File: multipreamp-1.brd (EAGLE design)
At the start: 100 x 50 mm, 132 parts, among them Q1 J201, Q2 J201, Q3 J201, Q4 J201, Q5 2N5088, Q6 J201, Q7 J201, Q8 J201

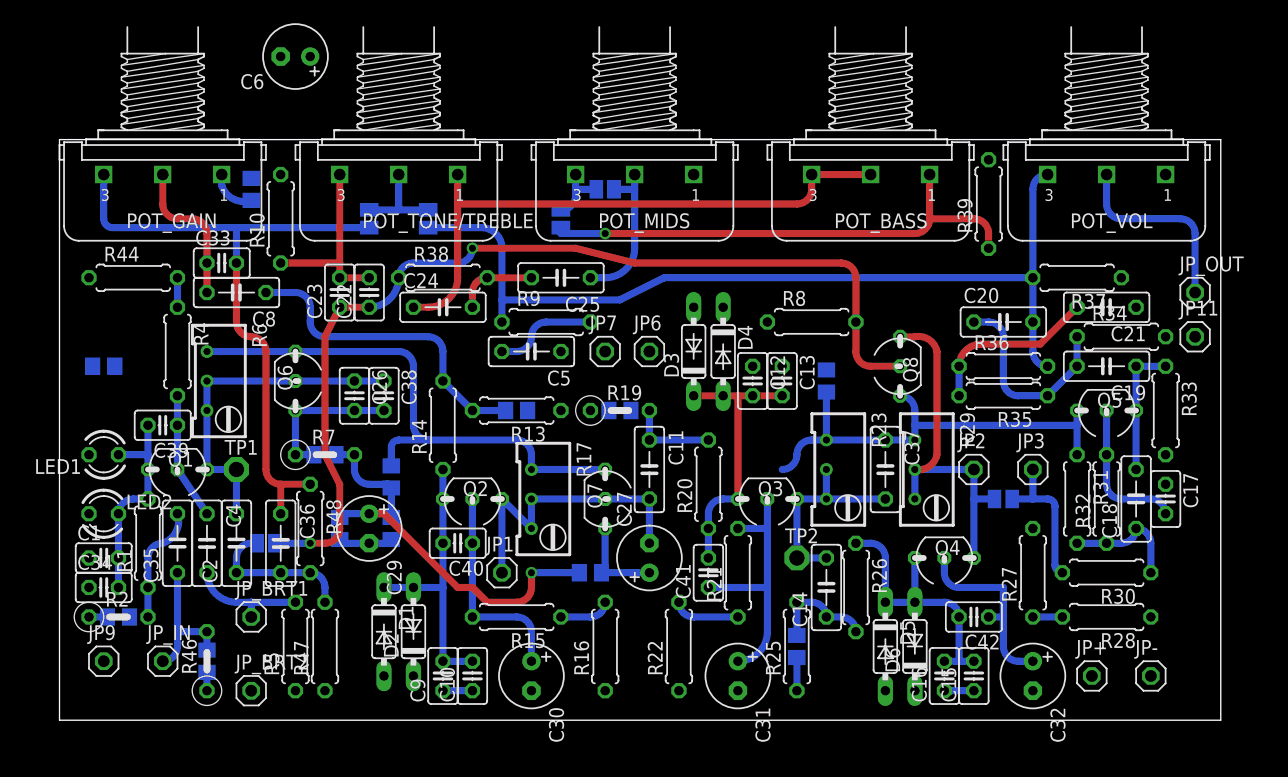
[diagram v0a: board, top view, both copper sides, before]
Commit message: Adicao de filtros RC na alimentacao (esquematico e layout)
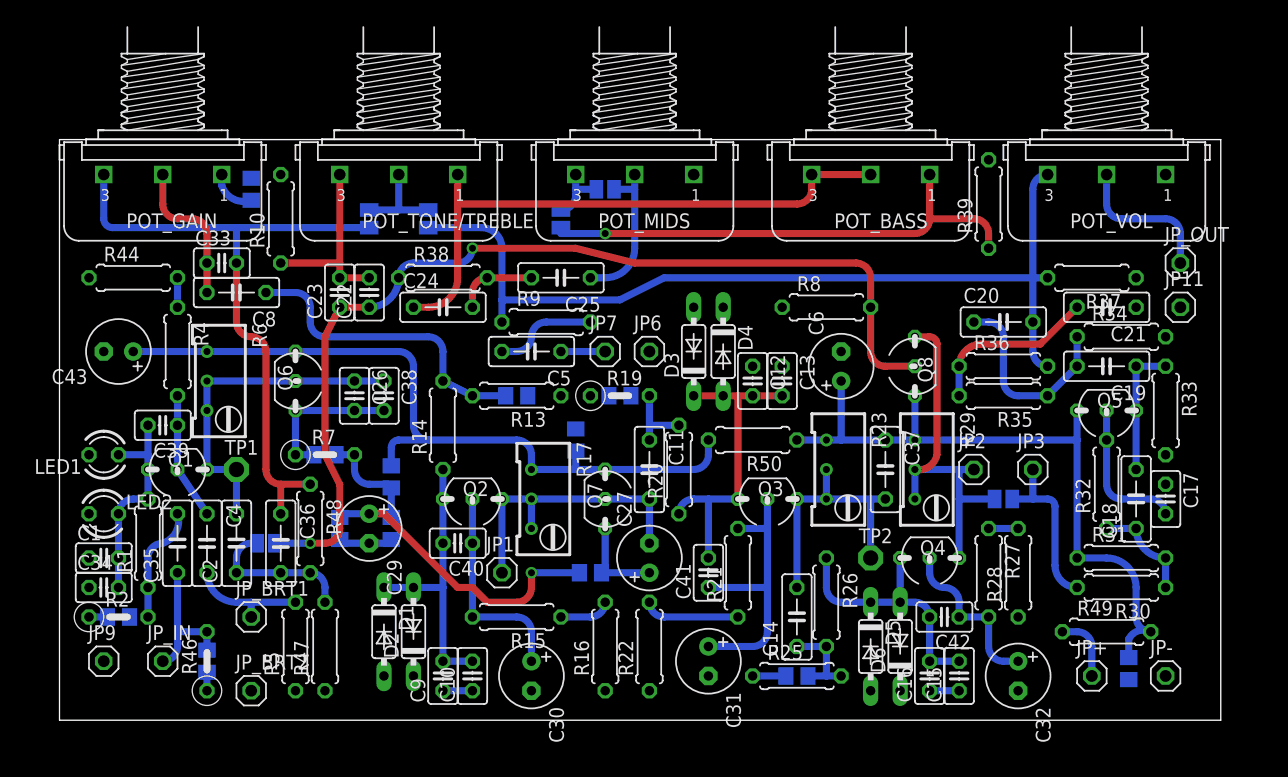
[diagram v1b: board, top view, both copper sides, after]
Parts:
- added C43: (no value), rcl:E2,5-6
- added R49, R50: (no value), rcl:0207/7
- moved C3 92.0 mm to (92.1, 4.45), turned to 270 degrees
- moved C6 54.0 mm to (67.3, 30.5), turned to 90 degrees
- moved C7 22.2 mm to (44.5, 24.1)
- moved R28 8.52 mm to (82.5, 12.7), turned to 90 degrees
- moved R31 6.35 mm to (91.4, 14.0), turned to 0 degrees
- moved TP2 6.35 mm to (69.8, 14.0)
- moved R27 3.81 mm to (80.0, 12.7), turned to 270 degrees
- moved C14 3.59 mm to (63.5, 8.89)
- moved JP11 2.84 mm to (96.5, 35.6)
- moved JP_OUT 2.84 mm to (96.5, 39.4)
- moved C31 2.84 mm to (55.9, 5.08)
- moved R20 2.84 mm to (53.3, 21.6)
- moved R26 2.84 mm to (66.0, 10.2)
- moved R22 2.54 mm to (50.8, 6.35)
- moved R24 2.54 mm to (63.5, 3.81), turned to 180 degrees
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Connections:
- new net 9V_1: C3.1, C37.1, C6.+, Q5.1, Q8.3, R23.1, R29.1, R31.1, R49.2, R50.1
- new net N$44: JP+.1, R49.1
- net GND: now also C43.-
- net V+: now also C43.+, R50.2; no longer C3.1, C37.1, C6.+, JP+.1, Q5.1, Q8.3, R23.1, R29.1, R31.1
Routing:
- net 9V_1: track 0.00 -> 59.8 mm
- net V+: track 86.3 -> 65.9 mm
- net N$44: track 0.00 -> 5.61 mm
- net N$22: track 17.8 -> 22.9 mm
- net N$35: track 16.3 -> 12.5 mm
- net N$14: track 0.00 -> 3.81 mm
- net N$19: track 23.4 -> 27.2 mm
- net N$21: track 5.61 -> 8.15 mm
- net N$20: track 22.6 -> 24.7 mm
- net N$26: track 16.3 -> 14.3 mm
- net N$29: track 12.5 -> 14.3 mm
- net N$9: track 77.2 -> 78.4 mm
- net N$23: track 9.94 -> 8.67 mm
- net N$25: track 23.9 -> 22.6 mm
- net N$18: track 7.62 -> 6.35 mm
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
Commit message: Alteracao no layout - troca de posicao entre pots de agudos e graves
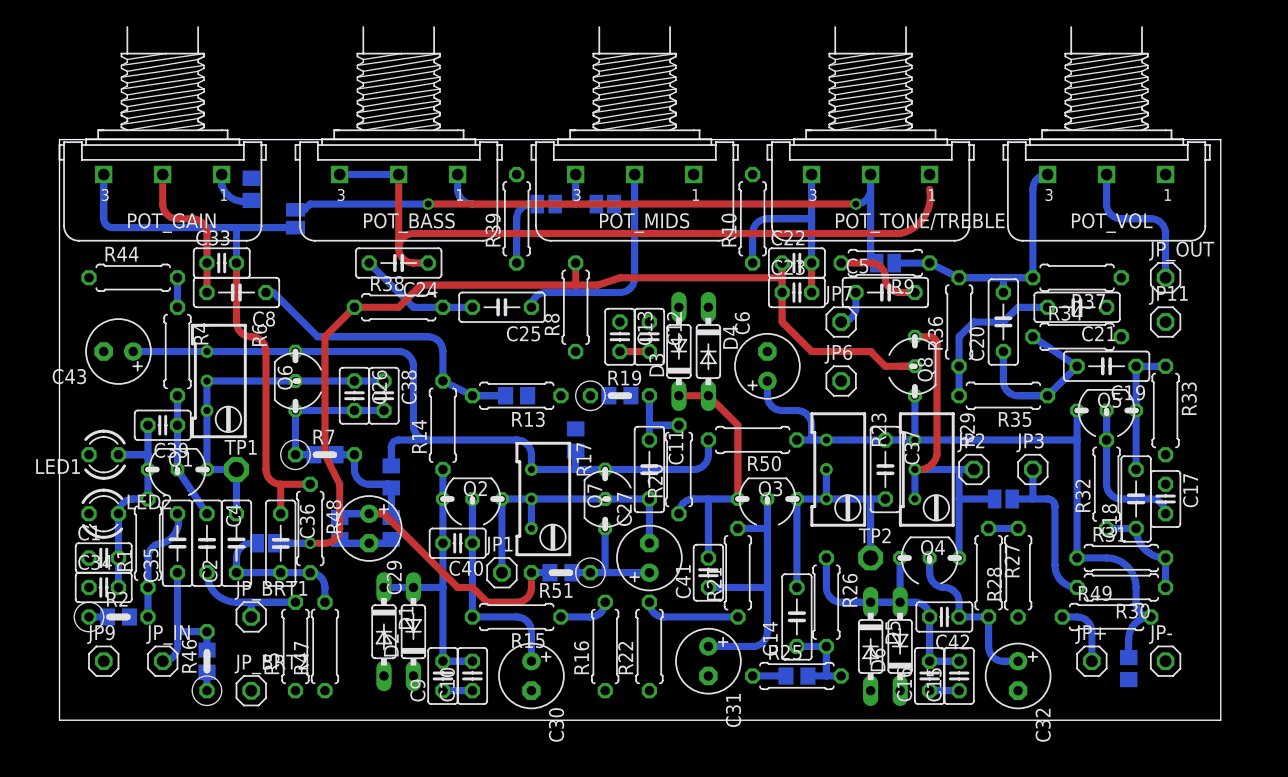
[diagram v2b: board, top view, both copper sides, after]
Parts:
- added R51: (no value), rcl:0207/5V
- moved R39 40.7 mm to (39.4, 43.2)
- moved R10 40.6 mm to (59.7, 43.2)
- moved POT_BASS 40.6 mm to (29.2, 47.0)
- moved POT_TONE/TREBLE 40.6 mm to (69.8, 47.0)
- moved SJ5 39.6 mm to (71.1, 39.4), turned to 180 degrees
- moved C23 39.4 mm to (63.5, 36.8), turned to 0 degrees
- moved C22 36.9 mm to (63.5, 39.4), turned to 0 degrees
- moved C5 30.9 mm to (71.1, 36.8), turned to 0 degrees
- moved R9 29.6 mm to (71.1, 39.4), turned to 180 degrees
- moved R8 21.6 mm to (44.5, 35.6), turned to 90 degrees
- moved JP7 20.5 mm to (67.3, 34.3)
- moved JP6 16.7 mm to (67.3, 29.2)
- moved C13 14.5 mm to (48.3, 33.0)
- moved C12 9.67 mm to (50.8, 33.0)
- moved C6 6.35 mm to (61.0, 30.5)
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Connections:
- net N$40: now also R51.1
- net VCC/2: now also R51.2
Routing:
- net N$9: track 78.4 -> 22.9 mm
- net TONE_OUT: track 8.13 -> 58.1 mm, vias 0 -> 2
- net N$43: track 43.5 -> 14.8 mm, vias 1 -> 0
- net TONE/TREBLE_1: track 51.1 -> 62.8 mm
- net N$6: track 13.0 -> 20.6 mm
- net N$11: track 55.7 -> 49.4 mm
- net N$36: track 6.88 -> 10.5 mm
- net VCC/2: track 37.0 -> 34.5 mm, vias 1 -> 0
- net N$40: track 8.07 -> 10.5 mm
- net N$32: track 17.3 -> 15.0 mm
- net TONE/TREBLE_3: track 16.5 -> 18.3 mm
- net 9V_1: track 59.8 -> 61.5 mm
- net N$19: track 27.2 -> 25.7 mm
- net N$10: track 8.67 -> 7.40 mm
- net N$33: track 14.8 -> 13.8 mm
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
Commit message: Alteracoes no layout - troca de encapsulamentos Renumeracao dos componentes
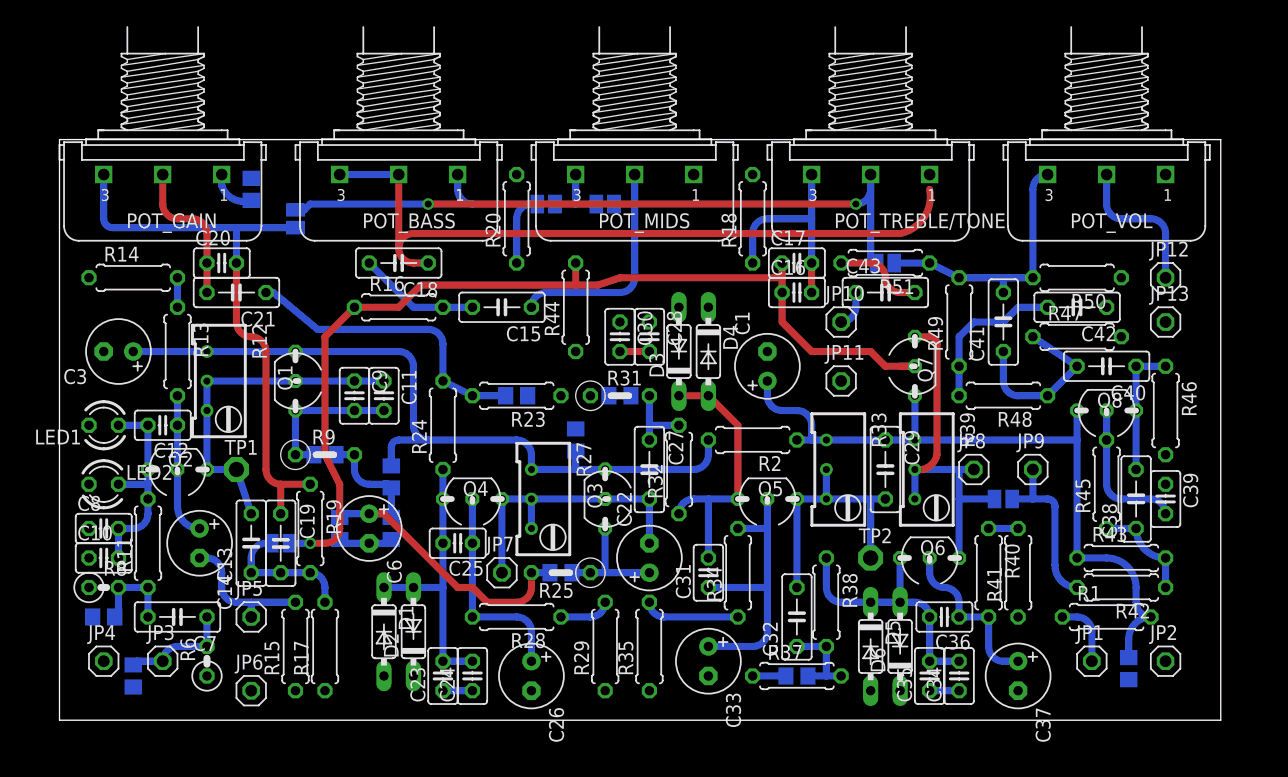
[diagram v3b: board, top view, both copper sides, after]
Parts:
- removed JP+, JP-, JP_BRT2, JP_IN: (no value), pinhead:1X01
- added JP10, JP13, JP4, JP8: (no value), pinhead:1X01
- C1, C22, C26, C33: device rcl:C025-025X050 -> rcl:E2,5-6
- C11, C20, C24, C25, C35, C36, C8: device rcl:C050-025X075 -> rcl:C025-025X050
- C13, C15, C38, C40, C41, C42: device rcl:C025-025X050 -> rcl:C050-025X075
- C14, C37: device rcl:C050-025X075 -> rcl:E2,5-6
- C2, C4, C5: value (none) -> 100n SMD; device rcl:C050-025X075 -> rcl:C0805
- C27, C29, C32, C43: device rcl:E2,5-6 -> rcl:C050-025X075
- C28: value 100n SMD -> (none); device rcl:C0805 -> rcl:C025-025X050
- C3: value 100n SMD -> (none); device rcl:C0805 -> rcl:E2,5-6
- C30, C31: device rcl:E2,5-6 -> rcl:C025-025X050
- C7: value 100n SMD -> (none); device rcl:C0805 -> rcl:C050-025X075
- Q5: value 2N5088 -> J201
- Q8: value J201 -> 2N5088
- R10, R22, R26, R30, R36, R5: value (none) -> 1M SMD; device rcl:0207/7 -> rcl:R0805
- R11: device rcl:R0805 -> rcl:0207/7
- R12: value 1M SMD -> (none); device rcl:R0805 -> rcl:RTRIM64W
- R17, R23, R29: device rcl:RTRIM64W -> rcl:0207/7
- R18, R24, R40, R41, R45: value 1M SMD -> (none); device rcl:R0805 -> rcl:0207/7
- R19, R2, R46, R51: device rcl:0207/5V -> rcl:0207/7
- R21: device rcl:0207/7 -> rcl:R0805
- R25, R31, R9: device rcl:0207/7 -> rcl:0207/5V
- R27, R33, R39: device rcl:0207/7 -> rcl:RTRIM64W
- R3: value 1M SMD -> 10k SMD
- R4: value (none) -> 10k SMD; device rcl:0207/7 -> rcl:R0805
- R42, R43: value 10k SMD -> (none); device rcl:R0805 -> rcl:0207/7
- R6: device rcl:RTRIM64W -> rcl:0207/2V
- R7: value (none) -> 1M SMD; device rcl:0207/5V -> rcl:R0805
- R8: device rcl:0207/7 -> rcl:0207/2V
- moved C3 91.2 mm to (5.08, 31.8), flipped to the top, turned to 180 degrees
- moved C39 86.6 mm to (95.2, 19.1), turned to 270 degrees
- moved R46 85.3 mm to (95.2, 26.7), turned to 270 degrees
- moved R1 82.8 mm to (90.2, 8.89), turned to 0 degrees
- moved JP9 81.7 mm to (83.8, 21.6)
- moved R45 79.0 mm to (90.2, 20.3), flipped to the top
- moved C2 77.6 mm to (92.1, 4.45), flipped to the bottom, turned to 270 degrees
- moved JP3 76.7 mm to (8.89, 5.08)
- moved C34 74.1 mm to (77.5, 3.81), turned to 90 degrees
- moved C19 72.7 mm to (19.1, 15.2), turned to 270 degrees
- moved C21 72.4 mm to (15.2, 36.8)
- moved R47 70.0 mm to (87.6, 33.0), turned to 0 degrees
- moved C20 67.5 mm to (14.0, 39.4), turned to 0 degrees
- moved C18 66.7 mm to (29.2, 39.4), turned to 180 degrees
- moved C43 66.2 mm to (71.1, 36.8), turned to 0 degrees
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- renumbered JP_BRT1 to JP5, JP_OUT to JP12, POT_TONE/TREBLE to POT_TREBLE/TONE
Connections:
- net 9V_1: now also C1.+, C2.1, C29.1, Q7.3, Q8.1, R1.2, R2.1, R33.1, R39.1, R43.1; no longer C3.1, C37.1, C6.+, Q5.1, Q8.3, R23.1, R29.1, R31.1, R49.2, R50.1
- net GND: now also C1.-, C2.2, C23.1, C24.1, C26.-, C28.1, C3.-, C30.1, C33.-, C35.1, C37.-, C39.1, C4.2, C42.1, C5.2, C8.1, JP13.1, JP2.1, JP4.1, R14.1, R15.1, R17.1, R18.2, R20.2, R21.1, R23.1, R29.1, R30.1, R31.1, R35.1, R36.1, R4.2, R41.1, R46.2, R47.2, R50.1, R6.1, R7.1; no longer C1.1, C12.1, C13.1, C15.1, C16.1, C17.1, C21.1, C28.2, C29.-, C3.2, C30.-, C31.-, C32.-, C43.-, C7.2, C9.1, JP-.1, JP9.1, JP_BRT2.1, R10.2, R11.1, R12.1, R13.1, R16.1, R18.1, R19.1, R2.1, R24.1, R25.1, R28.1, R3.1, R33.2, R34.2, R39.2, R43.2, R45.1, R46.1, R47.1
- net N$1: now also C14.-, R15.2; no longer C4.2, R5.2
- net N$10: now also C43.2, R51.2; no longer C5.2, R9.2
- net N$11: now also C19.1, C20.2, R19.1; no longer C33.2, C36.1, R48.1
- net N$12: now also R21.2; no longer R11.2
- net N$13: now also C21.1, R22.2, R23.2, R24.2; no longer C8.1, R12.2, R13.2, R14.2
- net N$14: now also C43.1, JP10.1; no longer C5.1, JP7.1
- net N$15: now also C22.-, C27.2, JP7.1, Q3.2, Q4.3, R27.2, R27.3; no longer C11.2, C27.-, JP1.1, Q2.3, Q7.2, R17.2, R17.3
- net N$16: now also C25.1, C26.+, Q4.2, R28.2; no longer C30.+, C40.1, Q2.2, R15.2
- net N$17: now also R28.1, R29.2; no longer R15.1, R16.2
- net N$18: now also C27.1, R30.2, R31.2, R32.2; no longer C11.1, R18.2, R19.2, R20.2
- net N$19: now also C28.2, C30.2, C31.2, Q5.1, R32.1; no longer C12.2, C13.2, C41.2, Q3.1, R20.1
- net N$2: now also C12.1, C14.+, Q2.2, R13.2; no longer C39.1, C4.1, Q1.2, R4.2
- net N$20: now also C31.1, C33.+, Q5.2, R34.2; no longer C31.+, C41.1, Q3.2, R21.2
- net N$21: now also R34.1, R35.2; no longer R21.1, R22.2
- net N$22: now also C29.2, C32.2, Q5.3, R33.2, R33.3; no longer C14.2, C37.2, Q3.3, R23.2, R23.3
- net N$23: now also C38.1, R42.1, R43.2, R45.1; no longer C18.1, R30.1, R31.2, R32.1
- net N$24: now also C32.1, R36.2, R37.2, R38.2; no longer C14.1, R24.2, R25.2, R26.2
- net N$25: now also C34.2, C35.2, C36.2, Q6.1, R38.1; no longer C15.2, C16.2, C42.2, Q4.1, R26.1
- net N$26: now also C36.1, C37.+, Q6.2, R40.2; no longer C32.+, C42.1, Q4.2, R27.2
- net N$27: now also R40.1, R41.2; no longer R27.1, R28.2
- net N$28: now also JP8.1, Q6.3, Q7.1, R39.2, R39.3, SJ5.1; no longer JP2.1, Q4.3, Q8.1, R29.2, R29.3, SJ2.1
- net N$29: now also JP9.1, R42.2, SJ5.2; no longer JP3.1, R30.2, SJ2.2
- net N$3: now also C20.1, C21.2; no longer C33.1, C8.2
- net N$30: now also C39.2, Q8.2, R45.2; no longer C17.2, Q5.2, R32.2
- net N$31: now also C38.2, C40.1, Q8.3, R46.1; no longer C18.2, C19.1, Q5.3, R33.1
- net N$32: now also C40.2, C41.1, R47.1, R48.1; no longer C19.2, C20.1, R34.1, R35.1
- net N$33: now also C42.2, R48.2, R49.1; no longer C21.2, R35.2, R36.1
- net N$34: now also R13.1, R14.2; no longer R4.1, R44.2
- net N$36: now also C15.2, C18.2, R16.2; no longer C24.2, C25.2, R38.2
- net N$37: now also SJ2.1, SJ3.1; no longer SJ1.1, SJ6.1
- net N$38: now also C7.1, JP3.1, R5.2, R6.2; no longer C35.1, JP_IN.1, R45.2, R46.2
- net N$39: now also C13.1, C19.2, R17.2, R19.2, SJ1.1; no longer C2.1, C36.2, R47.2, R48.2, SJ3.1
- net N$4: now also C10.2, C12.2, C8.2, Q2.1, R11.2; no longer C1.2, C34.2, C39.2, Q1.1, R1.2
- net N$40: now also C22.+, Q3.1, R25.1, R26.1; no longer C27.+, Q7.1, R41.1, R51.1
- net N$42: now also C23.2, C24.2, C25.2, Q4.1, R24.1; no longer C10.2, C40.2, C9.2, Q2.1, R14.1
- net N$43: now also R20.1, SJ3.2; no longer R39.1, SJ1.2
- net N$44: now also JP1.1, R1.1; no longer JP+.1, R49.1
- net N$5: now also C7.2, R11.1, R7.2, R8.2; no longer C35.2, R1.1, R2.2, R3.2
- net N$6: now also C15.1, SJ2.2; no longer C25.1, SJ6.2
- net N$7: now also C11.2, C9.2, Q1.1, R10.1, R9.1; no longer C26.2, C38.2, Q6.1, R40.1, R7.1
- net N$8: now also C11.1, C13.2, C9.1, Q1.2, Q2.3, R12.2, R12.3; no longer C2.2, C26.1, C38.1, Q1.3, Q6.2, R6.2, R6.3
- net N$9: now also C41.2, R49.2, R50.2, R51.1, SJ6.2; no longer C20.2, R36.2, R37.2, R9.1, SJ5.2
- net TONE/TREBLE_1: now also C18.1; no longer C24.1
- net TONE/TREBLE_3: now also C16.2, C17.2, R18.1; no longer C22.2, C23.2, R10.1
- net TONE_IN: now also C16.1, C17.1, Q7.2, R16.1, R44.2, SJ1.2; no longer C22.1, C23.1, Q8.2, R38.1, R8.2, SJ3.2
- net TONE_OUT: now also SJ6.1; no longer SJ5.1
- net V+: now also C3.+, C4.1, Q1.3, Q3.3, R12.1, R2.2, R27.1, R3.1; no longer C43.+, C7.1, Q6.3, Q7.3, R17.1, R42.1, R50.2, R6.1
- net VCC/2: now also C5.1, C6.+, R10.2, R25.2, R26.2, R3.2, R4.1, R9.2; no longer C28.1, C29.+, R40.2, R41.2, R42.2, R43.1, R51.2, R7.2
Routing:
- net GND: track 15.8 -> 12.7 mm
- net N$38: track 12.3 -> 9.55 mm
- net N$5: track 9.72 -> 7.75 mm
- net N$1: track 9.94 -> 11.8 mm
- net N$2: track 10.9 -> 12.2 mm
- net TONE_IN: track 85.5 -> 84.2 mm
- net N$39: track 13.0 -> 11.7 mm

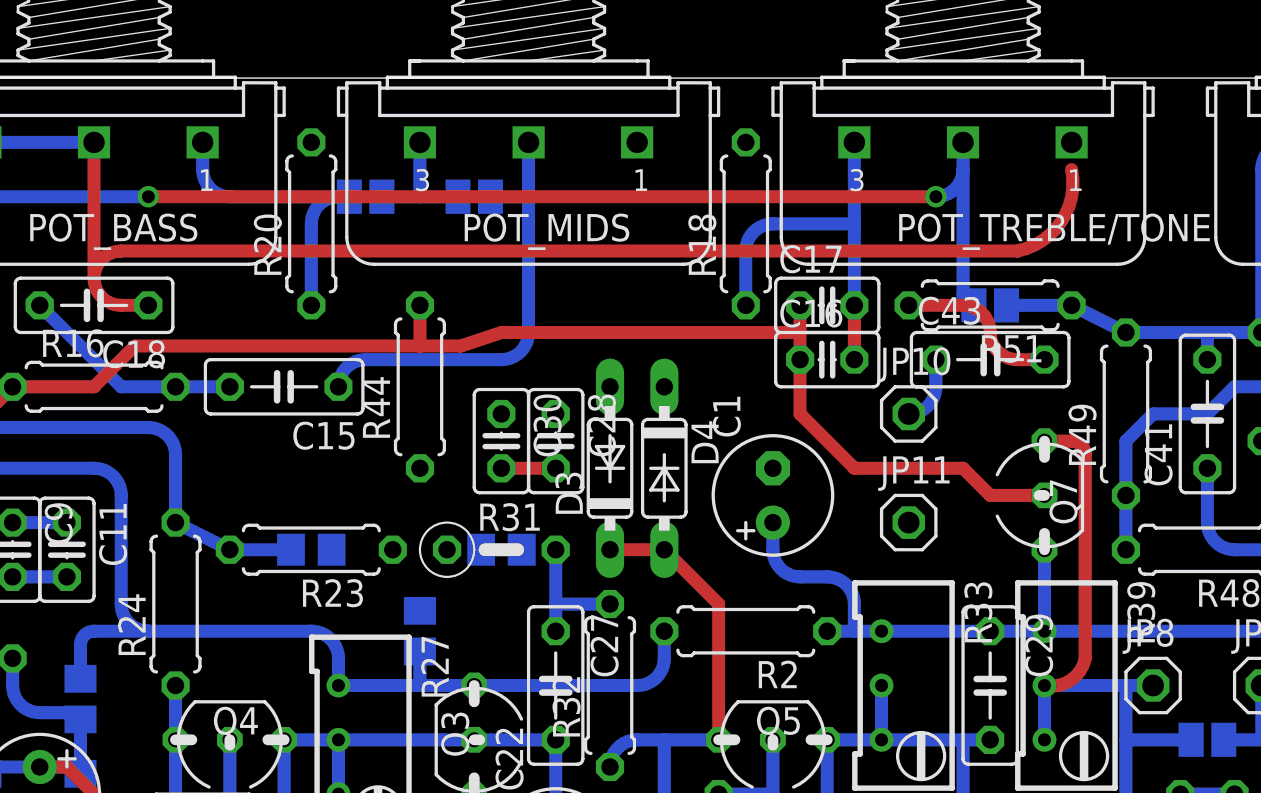
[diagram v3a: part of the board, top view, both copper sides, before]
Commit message: Alteracao no esquematico e layout - adicao de jumper para selecao da ligacao na saida do buffer JFET
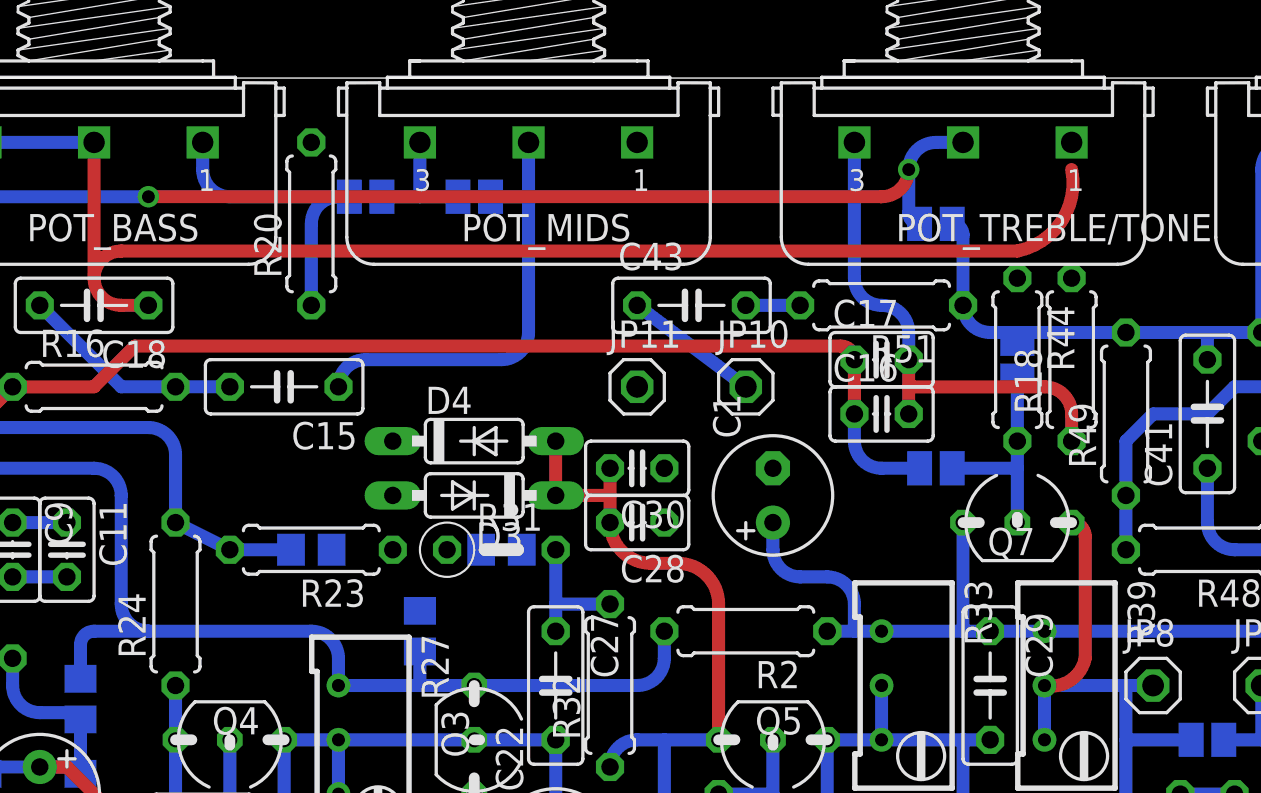
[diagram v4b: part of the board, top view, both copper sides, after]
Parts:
- added SJ7, SJ8: (no value), jumper:SJ
- moved R44 28.0 mm to (72.4, 36.8), turned to 270 degrees
- moved R18 16.5 mm to (74.9, 36.8)
- moved C43 14.2 mm to (57.1, 39.4)
- moved JP11 14.2 mm to (54.6, 35.6)
- moved D4 8.98 mm to (47.0, 33.0), turned to 0 degrees
- moved JP10 7.73 mm to (59.7, 35.6)
- moved C30 6.48 mm to (54.6, 31.8), turned to 180 degrees
- moved D3 6.48 mm to (47.0, 30.5), turned to 180 degrees
- moved C28 5.39 mm to (54.6, 29.2), turned to 180 degrees
- moved R51 5.08 mm to (66.0, 39.4)
- moved SJ6 4.58 mm to (68.6, 43.2)
- moved C16 3.59 mm to (66.0, 34.3)
- moved C17 3.59 mm to (66.0, 36.8)
- moved Q7 1.80 mm to (72.4, 29.2), turned to 0 degrees
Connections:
- new net N$45: Q7.2, R44.2, SJ7.1, SJ8.1
- net N$9: now also SJ7.2
- net TONE_IN: now also SJ8.2; no longer Q7.2, R44.2
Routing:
- net TONE_IN: track 84.2 -> 73.1 mm
- net N$45: track 0.00 -> 9.91 mm
- net N$9: track 22.9 -> 29.7 mm
- net N$19: track 25.7 -> 31.3 mm
- net N$28: track 32.3 -> 27.2 mm
- net TONE/TREBLE_3: track 18.3 -> 23.2 mm
- net N$10: track 7.40 -> 2.54 mm
- net TONE_OUT: track 58.1 -> 53.5 mm
- net N$14: track 3.07 -> 6.35 mm
- net 9V_1: track 61.5 -> 62.8 mm
